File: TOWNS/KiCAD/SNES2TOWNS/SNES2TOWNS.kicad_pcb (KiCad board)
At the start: 2 copper layers, 64.8 x 50.8 mm, 14 parts, among them J1 DE9_Receptacle, J6 SNES_CONTROLLER, J7 Slide Switch, J8 ArduinoNANOP1_P15, J9 ArduinoNANOP16_P30, U1 74LS157, U2 74LS157

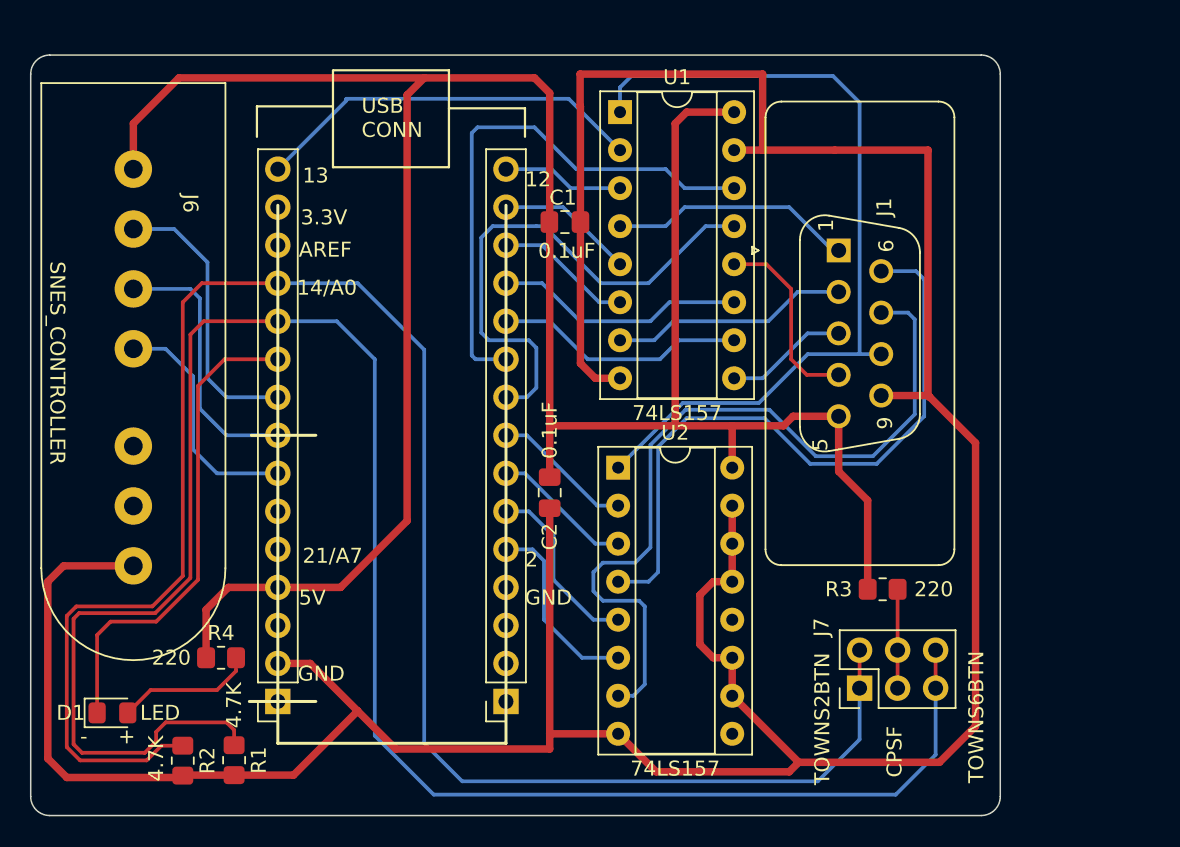
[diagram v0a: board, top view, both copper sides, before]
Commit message: Corrected orientation.
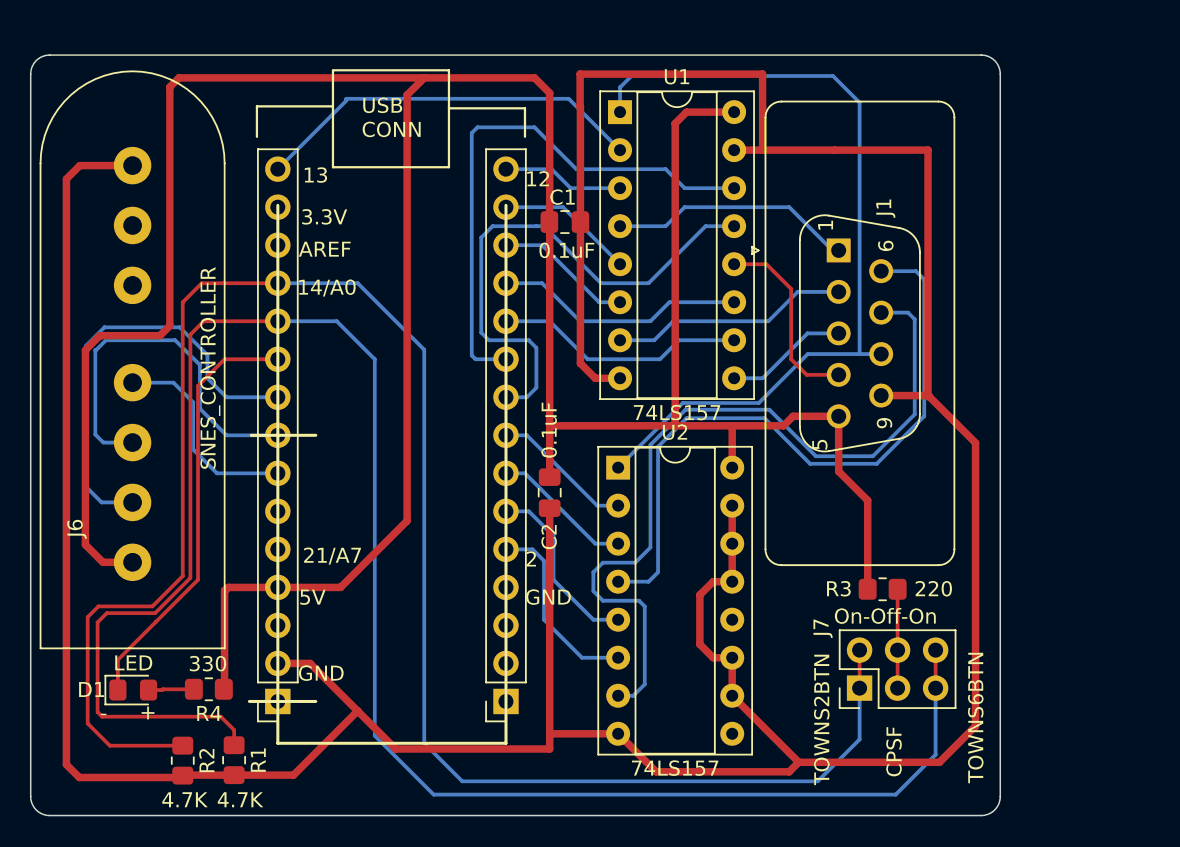
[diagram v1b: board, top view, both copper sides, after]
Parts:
- R4: value 220 -> 330
- moved J6 26.3 mm to (112.2, 97.4), turned to 90 degrees
- moved R4 2.26 mm to (117.3, 105.9), turned to 180 degrees
- moved D1 2.06 mm to (112.3, 105.9)
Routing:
- net +5V: track 166.5 -> 200.6 mm
- net GND: track 226.2 -> 250.8 mm
- net /CLOCK: track 18.8 -> 29.1 mm
- net /LATCH: track 18.0 -> 25.2 mm
- net /TWNS6BTN: track 133.1 -> 126.4 mm
- net Net-(D1-A): track 9.28 -> 3.05 mm
- net /TWNS2BTN: track 126.5 -> 121.9 mm
- net Net-(D1-K): track 32.5 -> 28.6 mm
- net /DATA: track 16.0 -> 14.1 mm
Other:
- board text added: "On-Off-On"

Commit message: Use PCM3TSMTR instead of general SPDT On-Off-On.
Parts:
- removed J7: Slide Switch, Connector_PinHeader_2.54mm:PinHeader_2x03_P2.54mm_Vertical
- added SW1: PCM13SMTR, Button_Switch_SMD:SW_SP3T_PCM13, F.Cu at (161.4, 105.1)
- R4: value 330 -> 220
- moved R3 0.46 mm to (161.9, 99.2)
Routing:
- net /TWNS6BTN: track 126.4 -> 134.3 mm, vias 0 -> 1
- net /TWNS2BTN: track 121.9 -> 124.5 mm, vias 0 -> 1
- net Net-(R3-Pad1): track 6.60 -> 4.52 mm
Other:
- board text added: "2BTN"
- board text added: "SNES Game Controller to FM TOWNS Adapter Ver. 20230907 by CaptainYS http://www.ysflight.com"
- board text added: "TW6BTN"
- board text removed: "On-Off-On"
- board text removed: "SNES Game Controller to FM TOWNS Adapter Ver. 20230903 by CaptainYS http://www.ysflight.com"
- board text removed: "TOWNS2BTN"
- board text removed: "TOWNS6BTN"

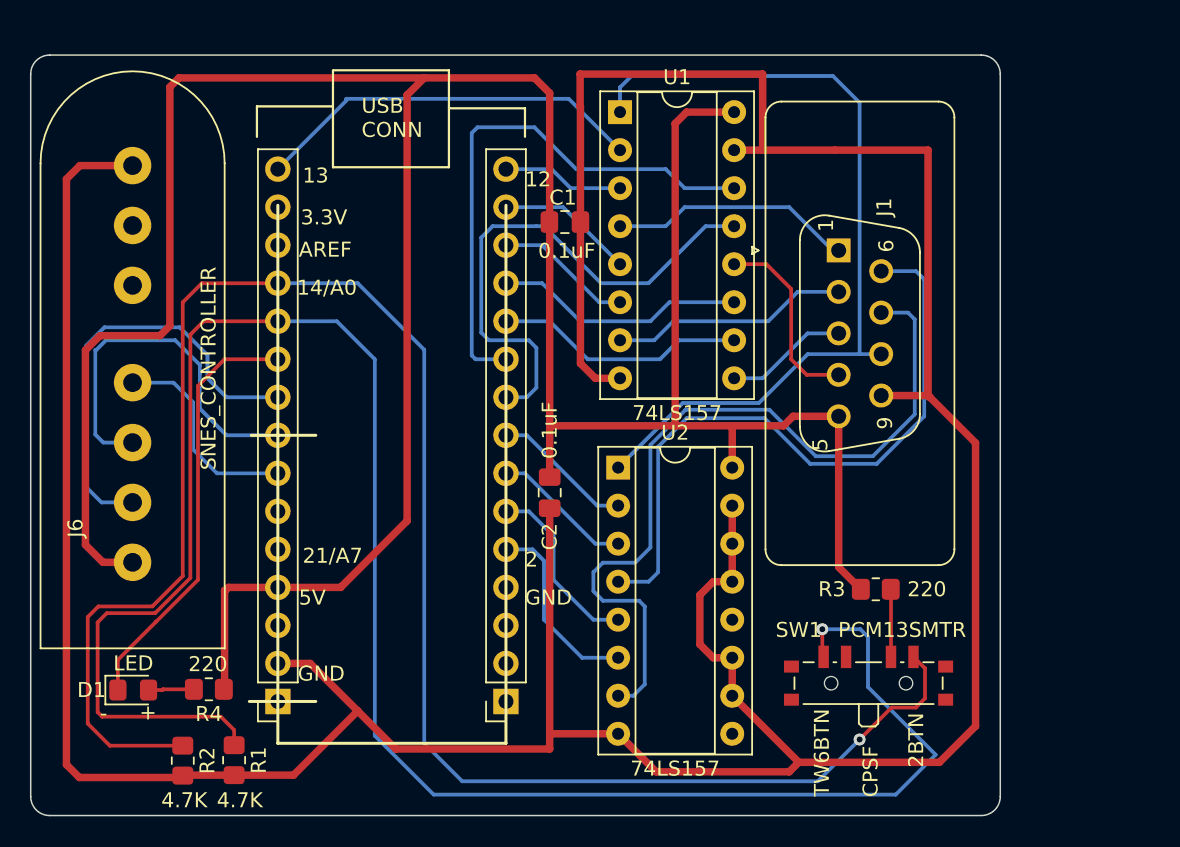
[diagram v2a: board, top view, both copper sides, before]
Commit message: Avoid pin 13 not to keep on-board LED on.  Pull-up (instead of ground) unused input pins of LS157.
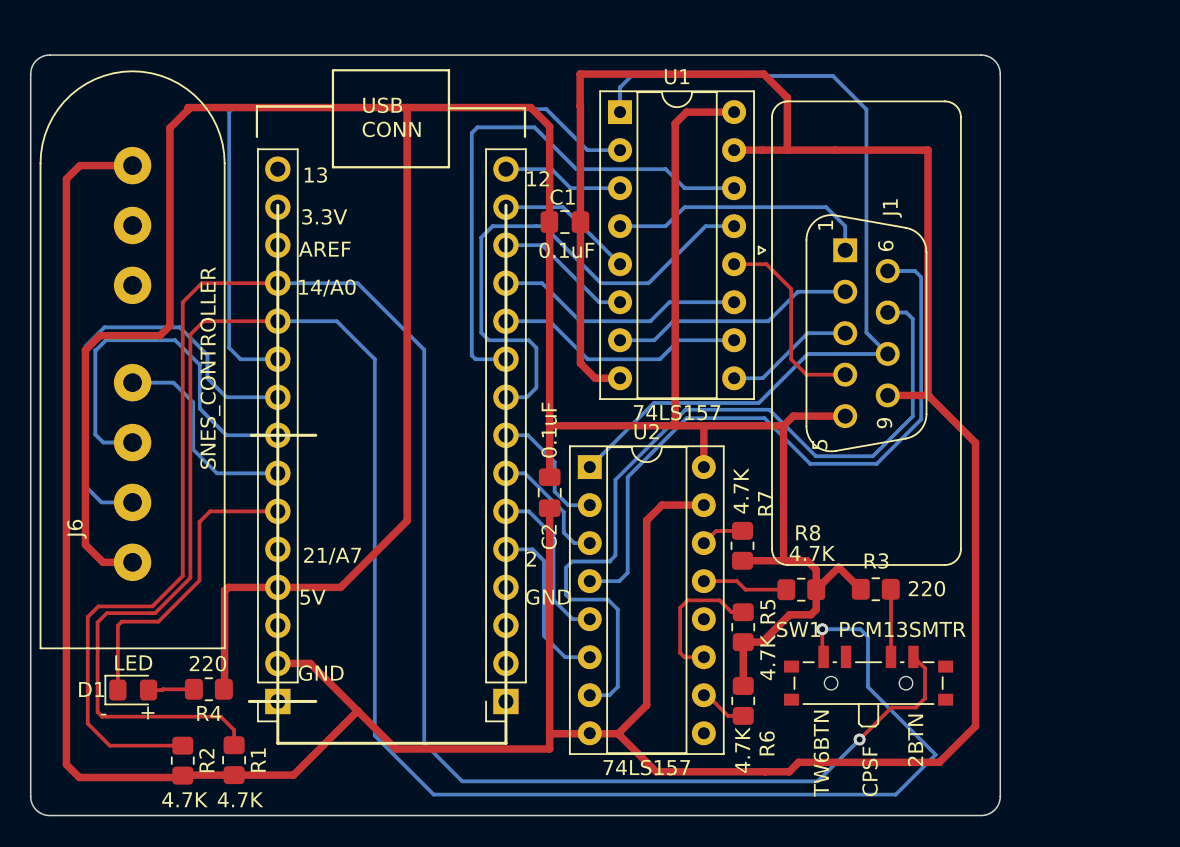
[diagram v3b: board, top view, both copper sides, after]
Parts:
- added R5: 4.7K, Resistor_SMD:R_0805_2012Metric_Pad1.20x1.40mm_HandSolder, F.Cu at (153.0, 101.7)
- added R6: 4.7K, Resistor_SMD:R_0805_2012Metric_Pad1.20x1.40mm_HandSolder, F.Cu at (153.0, 106.6)
- added R7: 4.7K, Resistor_SMD:R_0805_2012Metric_Pad1.20x1.40mm_HandSolder, F.Cu at (153.0, 96.3)
- added R8: 4.7K, Resistor_SMD:R_0805_2012Metric_Pad1.20x1.40mm_HandSolder, F.Cu at (156.9, 99.2)
- moved U2 1.90 mm to (142.8, 91.0)
- moved J1 0.44 mm to (159.8, 76.5)
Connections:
- J9 pad 10: Net-(D1-K) -> /OUT_P1A
- J9 pad 15: /OUT_P1A -> unconnected-(J9-Pin_15-Pad15)
- J9 pad 6: unconnected-(J9-Pin_6-Pad6) -> Net-(D1-K)
- U2 pad 10: GND -> Net-(U2-I1c)
- U2 pad 11: GND -> Net-(U2-I0c)
- U2 pad 13: GND -> Net-(U2-I1d)
- U2 pad 14: GND -> Net-(U2-I0d)
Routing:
- net /OUT_P1A: track 26.3 -> 46.6 mm
- net +5V: track 200.4 -> 211.5 mm
- net Net-(U2-I0c): track 0.00 -> 9.46 mm
- net Net-(D1-K): track 28.6 -> 20.4 mm
- net Net-(U2-I1d): track 0.00 -> 5.74 mm
- net Net-(U2-I1c): track 0.00 -> 3.20 mm
- net /COM: track 56.2 -> 59.3 mm
- net Net-(U2-I0d): track 0.00 -> 2.92 mm
- net GND: track 250.8 -> 248.1 mm
- net /OUT_P1: track 16.3 -> 17.7 mm
- net /OUT_P7B: track 12.8 -> 11.5 mm
- net /OUT_P7A: track 12.2 -> 11.1 mm
- net /OUT_P6B: track 9.44 -> 8.33 mm
- net /OUT_P6A: track 9.44 -> 8.69 mm
- net /OUT_P7: track 53.6 -> 54.2 mm
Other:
- board text added: "SNES Game Controller to FM TOWNS Adapter Ver. 20230910 by CaptainYS http://www.ysflight.com"
- board text removed: "SNES Game Controller to FM TOWNS Adapter Ver. 20230907 by CaptainYS http://www.ysflight.com"

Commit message: Gave up status LED.
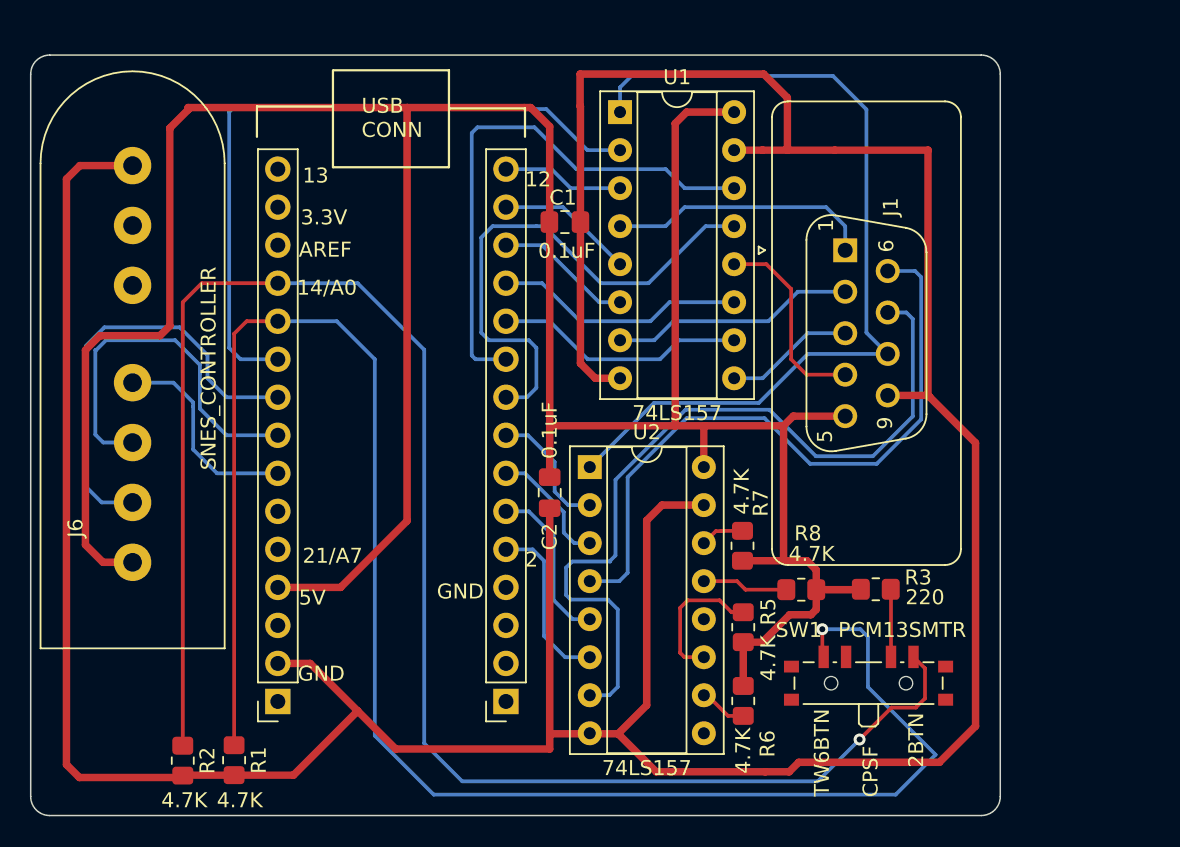
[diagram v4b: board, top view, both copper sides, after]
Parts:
- removed D1: LED, LED_SMD:LED_0805_2012Metric_Pad1.15x1.40mm_HandSolder
- removed R4: 220, Resistor_SMD:R_0805_2012Metric_Pad1.20x1.40mm_HandSolder
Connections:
- J9 pad 6: Net-(D1-K) -> unconnected-(J9-Pin_6-Pad6)
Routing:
- net Net-(D1-K): track 20.4 -> 0.00 mm
- net /TWNS6BTN: track 134.3 -> 118.5 mm
- net +5V: track 211.5 -> 200.0 mm
- net /TWNS2BTN: track 124.5 -> 114.3 mm
- net Net-(D1-A): track 3.05 -> 0.00 mm
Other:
- board text removed: "+"
- board text removed: "-"

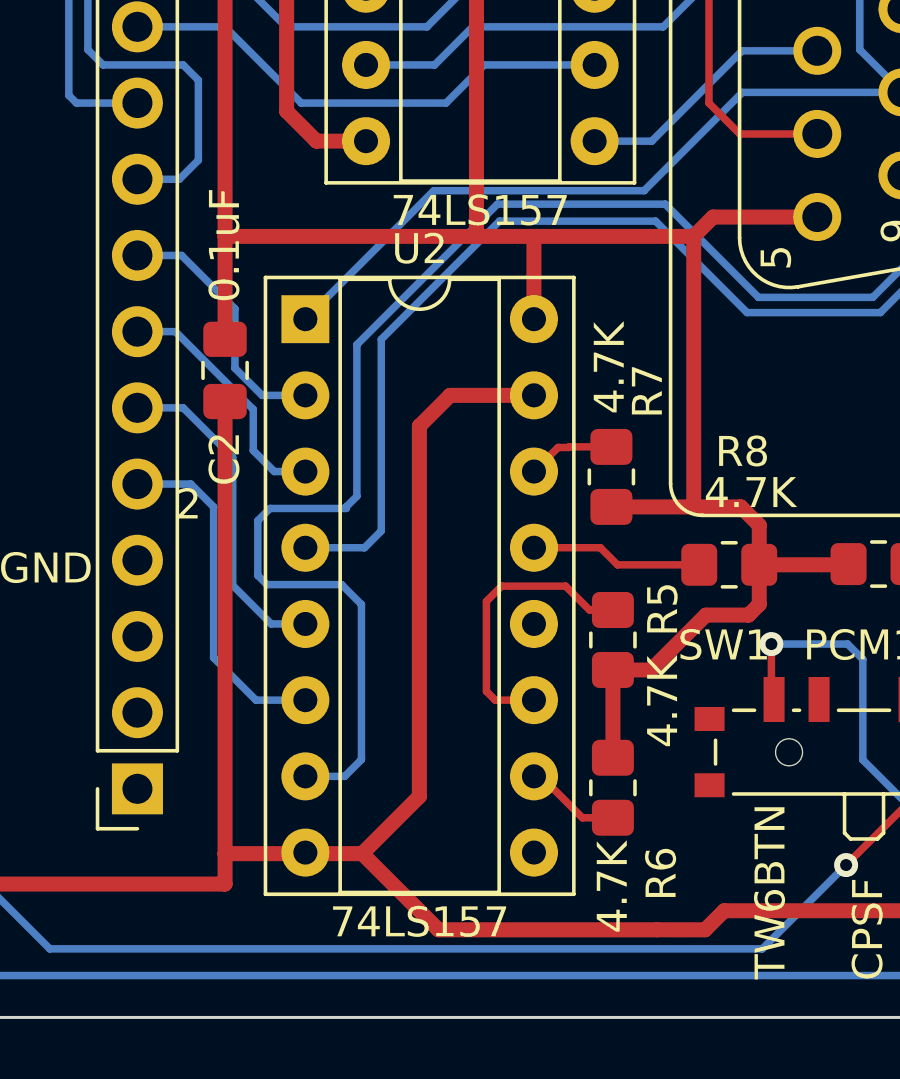
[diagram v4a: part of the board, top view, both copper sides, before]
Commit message: 74LS157 -> 74HC157
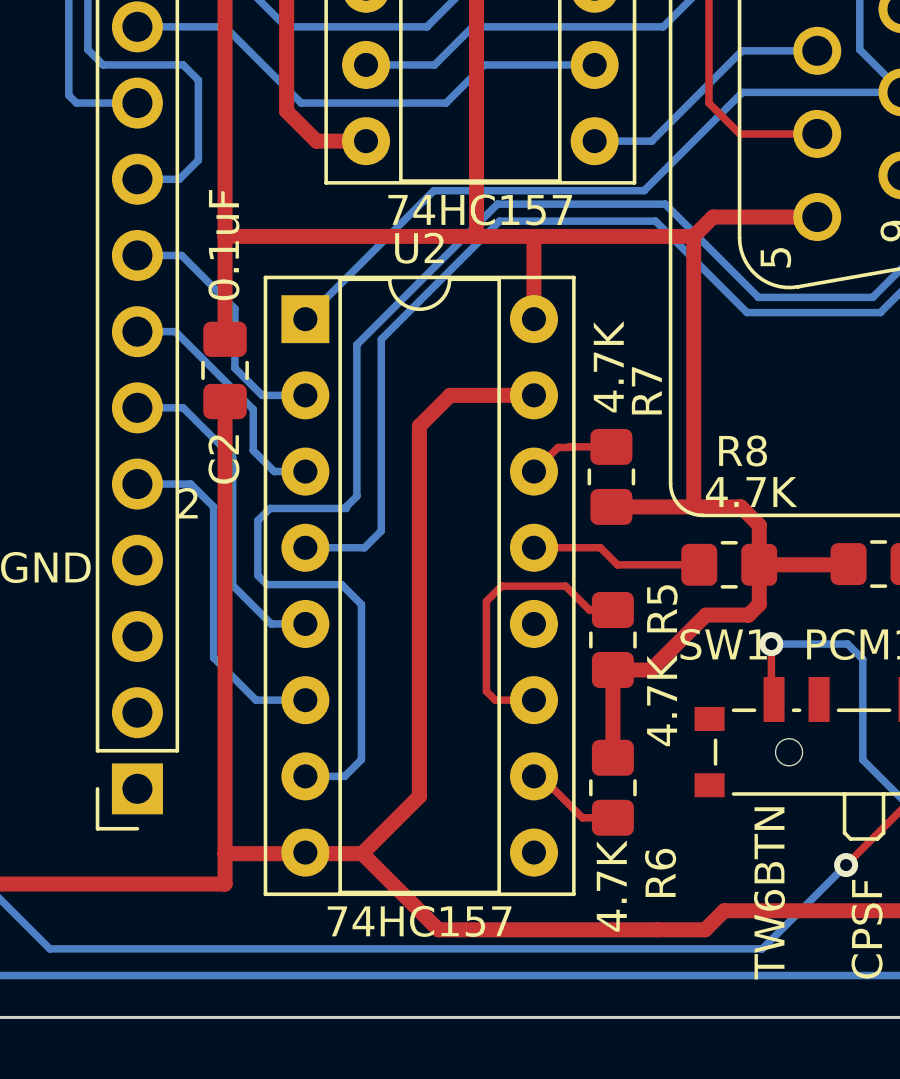
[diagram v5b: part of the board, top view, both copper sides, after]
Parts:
- U1, U2: value 74LS157 -> 74HC157
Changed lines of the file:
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@@
         (effects (font (size 1 1) (thickness 0.15)))
     )
-    (fp_text value "74LS157" (at 3.81 20.11) (layer "F.SilkS")
+    (fp_text value "74HC157" (at 3.81 20.11) (layer "F.SilkS")
         (effects (font (size 1 1) (thickness 0.15)))
     )
@@
         (effects (font (size 1 1) (thickness 0.15)))
     )
-    (fp_text value "74LS157" (at 3.81 20.11) (layer "F.SilkS")
+    (fp_text value "74HC157" (at 3.81 20.11) (layer "F.SilkS")
         (effects (font (size 1 1) (thickness 0.15)))
     )
@@
   (gr_line (start 105.41 64.77) (end 105.41 113.03)
     (stroke (width 0.1) (type default)) (layer "Edge.Cuts"))
-  (gr_text "SNES Game Controller to FM TOWNS Adapter\nVer. 20230910 by CaptainYS http://www.ysflight.com" (at 117.856 113.284) (layer "B.SilkS")
+  (gr_text "SNES Game Controller to FM TOWNS Adapter\nVer. 20230910 by CaptainYS http://www.ysflight.com" (at 117.856 113.3856) (layer "B.SilkS")
     (effects (font (size 1 1) (thickness 0.15)) (justify left bottom))
   )

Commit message: Updating PCB
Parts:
- added REF**: 2.85mm, MountingHole:MountingHole_3.2mm_M3, F.Cu at (109.1, 110.6)
- added REF**: 2.85mm, MountingHole:MountingHole_3.2mm_M3, F.Cu at (109.0, 67.1)
- added REF**: 2.85mm, MountingHole:MountingHole_3.2mm_M3, F.Cu at (170.8, 67.1)
- added REF**: 2.85mm, MountingHole:MountingHole_3.2mm_M3, F.Cu at (170.7, 110.7)
- R1, R2: value 4.7K -> 10K
- moved C1 9.79 mm to (137.7, 65.5)
- moved R7 9.20 mm to (152.3, 87.1), turned to -90 degrees
- moved J6 3.71 mm to (112.2, 101.1)
- moved U1 2.90 mm to (141.9, 67.3)
- moved J1 0.97 mm to (158.9, 76.5)
- moved SW1 0.53 mm to (160.9, 105.1)
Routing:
- net +5V: track 200.0 -> 155.9 mm
- net Net-(U2-I0d): track 2.92 -> 8.81 mm
- net /LATCH: track 25.2 -> 21.0 mm
- net /DATA: track 14.1 -> 10.7 mm
- net /OUT_P1B: track 8.15 -> 5.25 mm
- net /OUT_P3A: track 16.8 -> 14.2 mm
- net /OUT_P1: track 17.7 -> 20.2 mm
- net /OUT_P2A: track 9.20 -> 6.75 mm
- net /OUT_P4A: track 36.6 -> 34.3 mm
- net /OUT_P3B: track 16.8 -> 14.5 mm
- net /CLOCK: track 29.1 -> 27.2 mm
- net /OUT_P3: track 8.67 -> 10.6 mm
- net /OUT_P2: track 16.4 -> 18.3 mm
- net /OUT_P4B: track 35.8 -> 33.9 mm
- net /OUT_P2B: track 9.27 -> 7.43 mm
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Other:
- board size 64.8 x 50.8 mm -> 69.1 x 50.8 mm
- board text added: "SNES Game Controller to FM TOWNS Adapter Ver. 20231001 by CaptainYS http://www.ysflight.com"
- board text removed: "SNES Game Controller to FM TOWNS Adapter Ver. 20230910 by CaptainYS http://www.ysflight.com"

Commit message: Updated PCB
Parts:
- moved R7 19.9 mm to (162.3, 104.3), turned to 0 degrees
- moved C2 19.6 mm to (132.7, 110.9)
- moved REF** 8.33 mm to (117.3, 67.2)
- moved SW1 4.46 mm to (158.9, 109.1)
- moved R6 4.00 mm to (156.2, 104.3), turned to 180 degrees
- moved R5 3.24 mm to (156.2, 101.8), turned to 180 degrees
- moved REF** 2.29 mm to (168.6, 67.1)
- moved J1 2.18 mm to (156.7, 76.4)
- moved REF** 1.93 mm to (168.8, 110.7)
- moved U2 0.87 mm to (141.9, 91.0)
- moved C1 0.82 mm to (137.2, 66.1), turned to 90 degrees
- moved R3 0.78 mm to (162.6, 99.2)
- moved R8 0.64 mm to (156.2, 99.2)
- moved J6 0.56 mm to (111.7, 101.1)
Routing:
- net GND: track 249.4 -> 222.6 mm
- net Net-(U2-I0d): track 8.81 -> 33.4 mm
- net /TWNS6BTN: track 117.1 -> 95.7 mm
- net +5V: track 155.9 -> 175.5 mm
- net Net-(R3-Pad1): track 4.75 -> 13.1 mm
- net /OUT_P1: track 20.2 -> 16.5 mm
- net /TWNS2BTN: track 114.5 -> 111.1 mm
- net Net-(U2-I1c): track 3.20 -> 6.57 mm
- net Net-(U2-I0c): track 9.46 -> 6.57 mm
- net /OUT_P1A: track 44.9 -> 42.4 mm
- net /OUT_P3: track 10.6 -> 8.46 mm
- net /OUT_P2: track 18.3 -> 16.2 mm
- net /OUT_P4: track 15.0 -> 13.2 mm
- net /OUT_P6: track 45.8 -> 44.6 mm
- net /OUT_P6A: track 8.69 -> 7.80 mm
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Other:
- board size 69.1 x 50.8 mm -> 67 x 50.8 mm
- board text added: "SNES Game Controller to FM TOWNS Adapter Ver. 20231002 by CaptainYS http://www.ysflight.com"
- board text removed: "SNES Game Controller to FM TOWNS Adapter Ver. 20231001 by CaptainYS http://www.ysflight.com"
